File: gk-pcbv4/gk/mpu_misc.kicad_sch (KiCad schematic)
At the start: 28 parts, among them J5 Conn_ARM_Cortex_Debug_ETM_20, SW1 SW_Push, SW2 DS04-254-[12]-04BK-SMT, U5 STM32MP255DAI3, Y1 24MHz, Y2 CM8V-T1A-32.768kHz-12.5pF-20P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

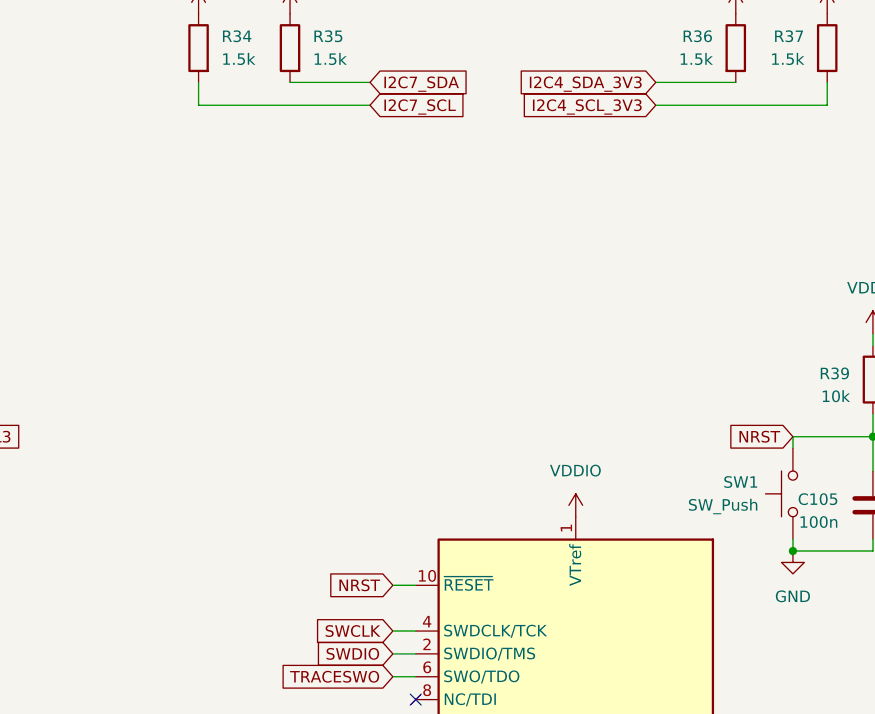
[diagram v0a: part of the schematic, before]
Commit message: add back-side 10 pin debug header
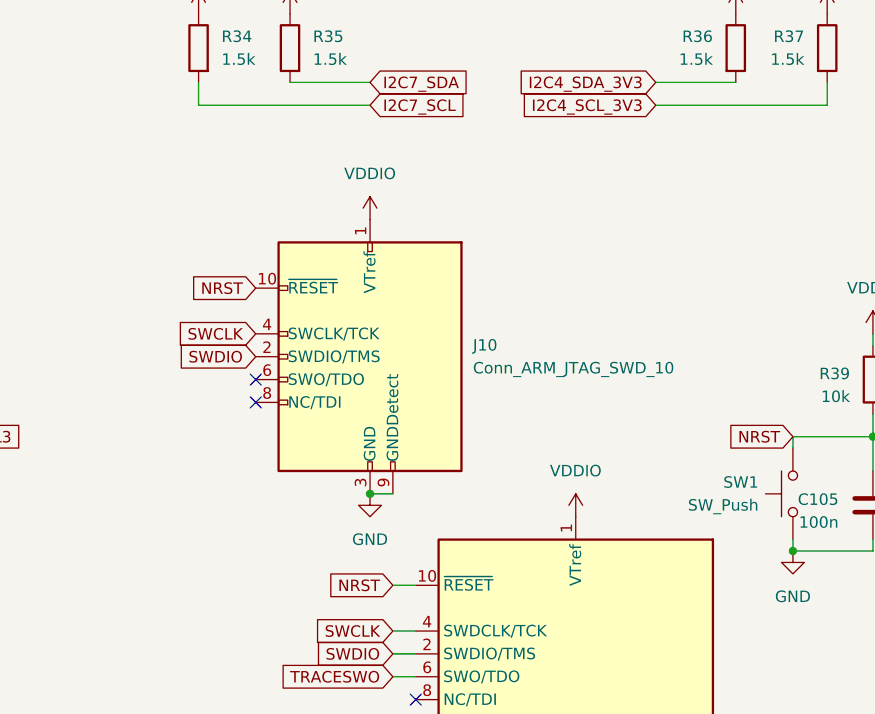
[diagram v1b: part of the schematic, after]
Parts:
- added J10: Conn_ARM_JTAG_SWD_10, Connector_PinHeader_1.27mm:PinHeader_2x05_P1.27mm_Vertical_SMD, symbol Connector:Conn_ARM_JTAG_SWD_10
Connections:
- net GND: now also J10.3 (GND), J10.5 (GND), J10.9 (GNDDetect)
- net NRST: now also J10.10 (~{RESET})
- net SWCLK: now also J10.4 (SWCLK/TCK)
- net SWDIO: now also J10.2 (SWDIO/TMS)
- net VDDIO: now also J10.1 (VTref)
- no-connect marks 32 -> 34

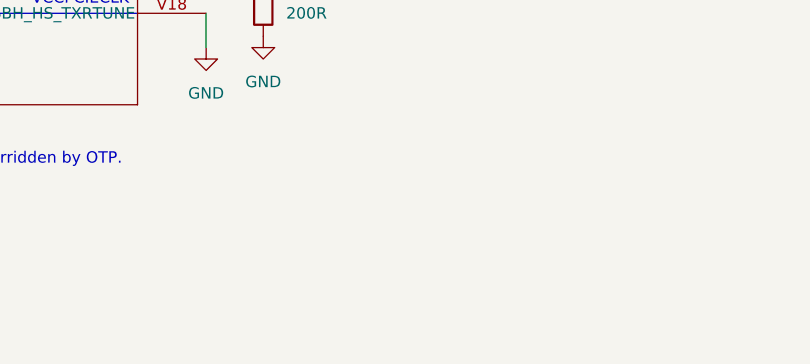
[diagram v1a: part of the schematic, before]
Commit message: Add UART6 out for debug
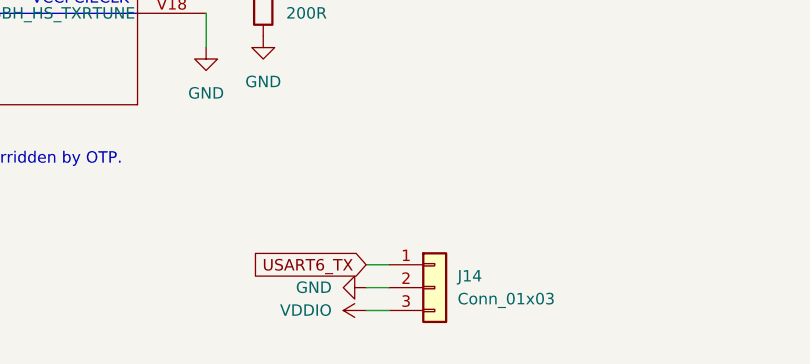
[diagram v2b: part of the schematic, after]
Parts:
- added J14: Conn_01x03, Connector_PinSocket_2.54mm:PinSocket_1x03_P2.54mm_Vertical, symbol Connector_Generic:Conn_01x03
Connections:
- net GND: now also J14.2 (Pin_2)
- net VDDIO: now also J14.3 (Pin_3)
- new net USART6_TX: J14.1 (Pin_1)

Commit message: pcb order 20251115
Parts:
- removed R42, R43, R44: 1k, Resistor_SMD:R_0603_1608Metric, symbol Device:R
- removed SW2: DS04-254-[12]-04BK-SMT, Button_Switch_SMD:SW_DIP_SPSTx04_Slide_9.78x12.34mm_W8.61mm_P2.54mm, symbol Switch:SW_DIP_x04
- added SW2: SW_Push, Button_Switch_SMD:SW_SPST_PTS647_Sx38, symbol Switch:SW_Push
- SW1: footprint gk-pcbv3:Tactile Switch 6x3.5mm -> Button_Switch_SMD:SW_SPST_PTS647_Sx38
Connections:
- net BOOT3: now also SW2.2
- net VDDIO: now also R45.1; no longer R45.2
- new net: R45.2, SW2.1
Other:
- moved on the sheet: R45

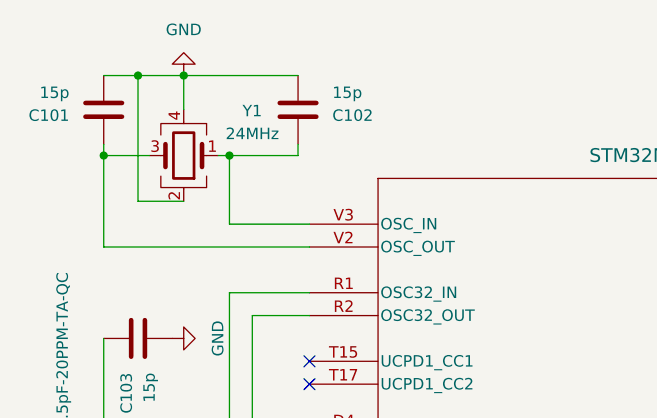
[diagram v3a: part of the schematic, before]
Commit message: Change HSE to 40 MHz as per EV1
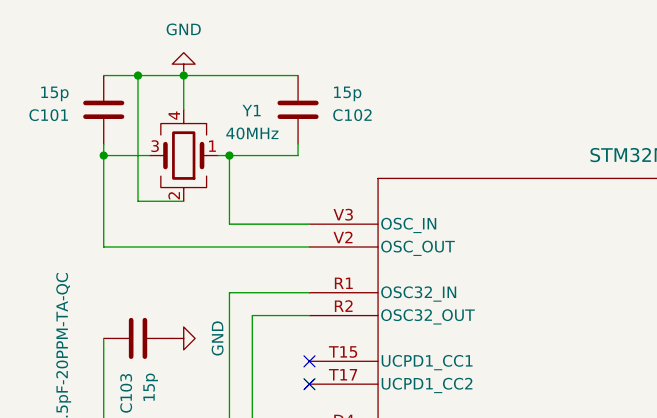
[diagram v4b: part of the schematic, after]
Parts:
- Y1: value 24MHz -> 40MHz
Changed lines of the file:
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@@
 			)
 		)
-		(property "Value" "24MHz"
+		(property "Value" "40MHz"
 			(at 39.37 26.7968 0)
 			(effects

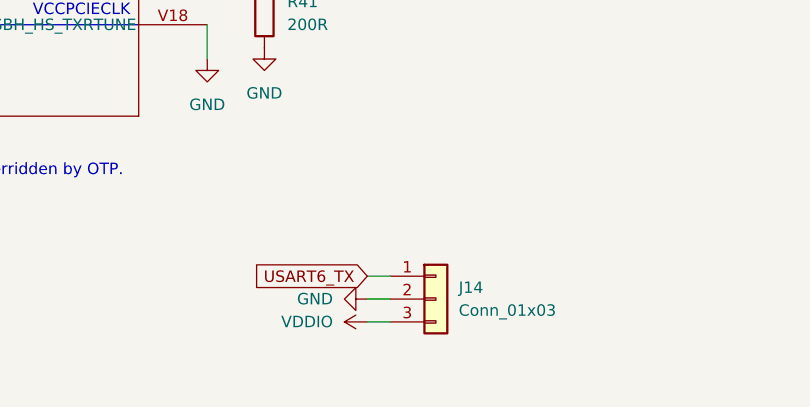
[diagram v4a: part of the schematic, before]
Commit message: add usart6 connection to schematic
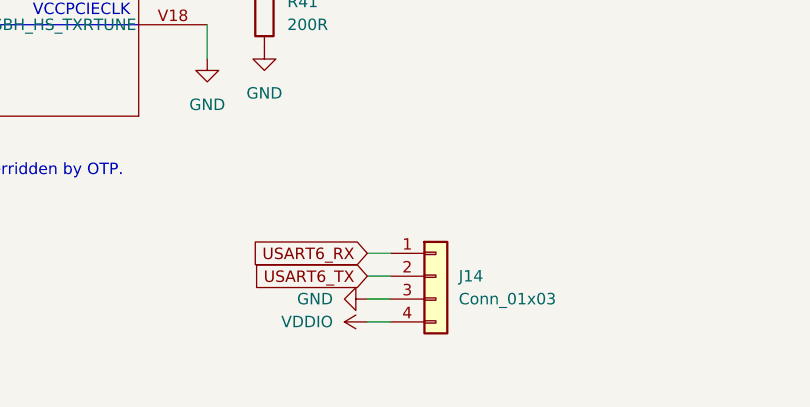
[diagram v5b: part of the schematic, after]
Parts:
- J14: symbol Connector_Generic:Conn_01x03 -> Connector_Generic:Conn_01x04
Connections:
- net GND: now also J14.3 (Pin_3); no longer J14.2 (Pin_2)
- net USART6_TX: now also J14.2 (Pin_2); no longer J14.1 (Pin_1)
- net VDDIO: now also J14.4 (Pin_4); no longer J14.3 (Pin_3)
- new net USART6_RX: J14.1 (Pin_1)
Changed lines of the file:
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@@
 	(wire
 		(pts
+			(xy 147.32 179.07) (xy 144.78 179.07)
+		)
+		(stroke
+			(width 0)
+			(type default)
+		)
+	)
+	(wire
+		(pts
 			(xy 236.22 157.48) (xy 242.57 157.48)
 		)
@@
 	(wire
 		(pts
-			(xy 144.78 173.99) (xy 147.32 173.99)
-		)
-		(stroke
-			(width 0)
-			(type default)
-		)
-	)
-	(wire
-		(pts
 			(xy 236.22 152.4) (xy 236.22 157.48)
 		)
@@
 	(wire
 		(pts
+			(xy 147.32 176.53) (xy 144.78 176.53)
+		)
+		(stroke
+			(width 0)
+			(type default)
+		)
+	)
+	(wire
+		(pts
 			(xy 233.68 152.4) (xy 233.68 158.75)
 		)
@@
 	(wire
 		(pts
-			(xy 147.32 176.53) (xy 144.78 176.53)
+			(xy 242.57 36.83) (xy 261.62 36.83)
 		)
 		(stroke
@@
 	(wire
 		(pts
-			(xy 242.57 36.83) (xy 261.62 36.83)
+			(xy 213.36 142.24) (xy 213.36 144.78)
 		)
 		(stroke
@@
 	(wire
 		(pts
-			(xy 213.36 142.24) (xy 213.36 144.78)
+			(xy 213.36 129.54) (xy 215.9 129.54)
 		)
 		(stroke
@@
 	(wire
 		(pts
-			(xy 213.36 129.54) (xy 215.9 129.54)
+			(xy 36.83 36.83) (xy 45.72 36.83)
 		)
 		(stroke
@@
 	(wire
 		(pts
-			(xy 36.83 36.83) (xy 45.72 36.83)
+			(xy 213.36 144.78) (xy 215.9 144.78)
 		)
 		(stroke
@@
 	(wire
 		(pts
-			(xy 213.36 144.78) (xy 215.9 144.78)
+			(xy 213.36 127) (xy 215.9 127)
 		)
 		(stroke
@@
 	(wire
 		(pts
-			(xy 213.36 127) (xy 215.9 127)
+			(xy 147.32 173.99) (xy 144.78 173.99)
 		)
 		(stroke
@@
 	(wire
 		(pts
-			(xy 213.36 132.08) (xy 215.9 132.08)
+			(xy 144.78 171.45) (xy 147.32 171.45)
 		)
 		(stroke
@@
 	(wire
 		(pts
-			(xy 144.78 179.07) (xy 147.32 179.07)
+			(xy 213.36 132.08) (xy 215.9 132.08)
 		)
 		(stroke
@@
 		)
 	)
+	(global_label "USART6_RX"
+		(shape input)
+		(at 144.78 171.45 180)
+		(fields_autoplaced yes)
+		(effects
+			(font
+				(size 1.27 1.27)
+			)
+			(justify right)
+		)
+		(property "Intersheetrefs" "${INTERSHEET_REFS}"
+			(at 131.272 171.45 0)
+			(effects
+				(font
+					(size 1.27 1.27)
+				)
+				(justify right)
+				(hide yes)
+			)
+		)
+	)
 	(global_label "TRACESWO"
 		(shape input)
@@
 	)
 	(symbol
-		(lib_id "Connector_Generic:Conn_01x03")
-		(at 152.4 176.53 0)
+		(lib_id "Connector_Generic:Conn_01x04")
+		(at 152.4 173.99 0)
 		(unit 1)
 		(exclude_from_sim no)
@@
 		(fields_autoplaced yes)
 		(property "Reference" "J14"
-			(at 154.94 175.2599 0)
+			(at 154.94 173.9899 0)
 			(effects
 				(font
@@
 		)
 		(property "Value" "Conn_01x03"
-			(at 154.94 177.7999 0)
+			(at 154.94 176.5299 0)
 			(effects
 				(font
@@
 		)
 		(property "Footprint" "Connector_PinSocket_2.54mm:PinSocket_1x03_P2.54mm_Vertical"
-			(at 152.4 176.53 0)
+			(at 152.4 173.99 0)
 			(effects
 				(font
@@
 		)
 		(property "Datasheet" "~"
-			(at 152.4 176.53 0)
+			(at 152.4 173.99 0)
 			(effects
 				(font
@@
 			)
 		)
-		(property "Description" "Generic connector, single row, 01x03, script generated (kicad-library-utils/schlib/autogen/connector/)"
-			(at 152.4 176.53 0)
+		(property "Description" "Generic connector, single row, 01x04, script generated (kicad-library-utils/schlib/autogen/connector/)"
+			(at 152.4 173.99 0)
 			(effects
 				(font
@@
 		(pin "3"
 		)
+		(pin "4"
+		)
 		(instances

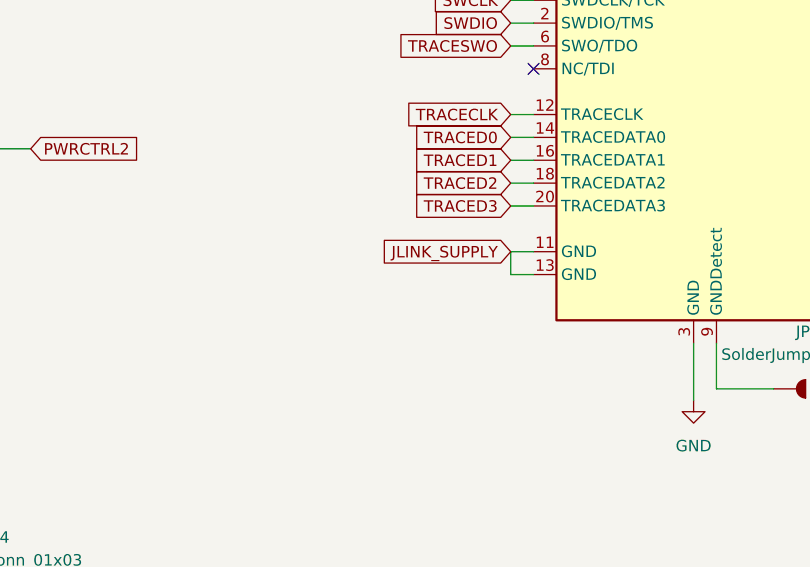
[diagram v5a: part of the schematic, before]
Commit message: Remove wakeupn mosfets in schematic
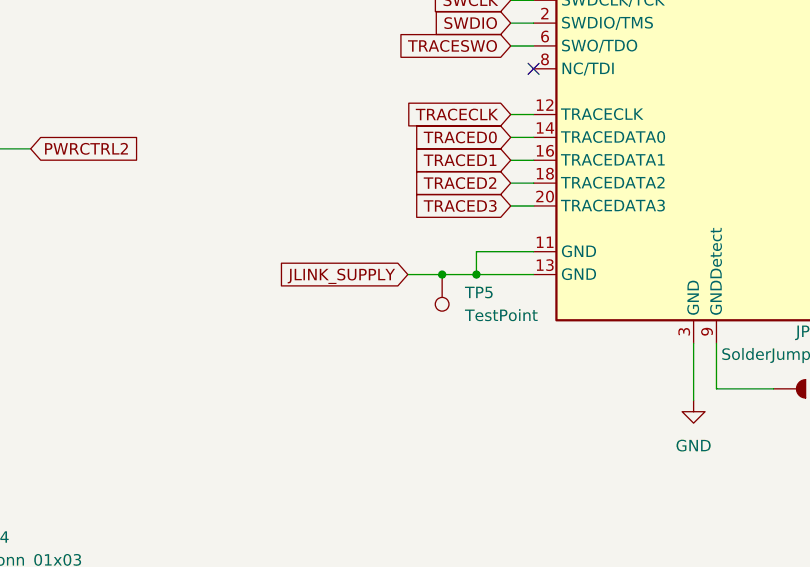
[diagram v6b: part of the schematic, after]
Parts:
- added TP5: TestPoint, Connector_PinHeader_2.54mm:PinHeader_1x01_P2.54mm_Vertical, symbol Connector:TestPoint
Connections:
- net JLINK_SUPPLY: now also TP5.1
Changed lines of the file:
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@@
 	)
 	(junction
+		(at 209.55 144.78)
+		(diameter 0)
+		(color 0 0 0 0)
+	)
+	(junction
 		(at 36.83 29.21)
 		(diameter 0)
@@
 	)
 	(junction
+		(at 205.74 144.78)
+		(diameter 0)
+		(color 0 0 0 0)
+	)
+	(junction
 		(at 152.4 130.81)
 		(diameter 0)
@@
 	(wire
 		(pts
+			(xy 209.55 142.24) (xy 215.9 142.24)
+		)
+		(stroke
+			(width 0)
+			(type default)
+		)
+	)
+	(wire
+		(pts
 			(xy 213.36 137.16) (xy 215.9 137.16)
 		)
@@
 	(wire
 		(pts
-			(xy 213.36 142.24) (xy 215.9 142.24)
+			(xy 201.93 144.78) (xy 205.74 144.78)
 		)
 		(stroke
@@
 	(wire
 		(pts
-			(xy 213.36 142.24) (xy 213.36 144.78)
+			(xy 209.55 144.78) (xy 209.55 142.24)
 		)
 		(stroke
@@
 	(wire
 		(pts
-			(xy 36.83 36.83) (xy 45.72 36.83)
+			(xy 209.55 144.78) (xy 215.9 144.78)
+		)
+		(stroke
+			(width 0)
+			(type default)
+		)
+	)
+	(wire
+		(pts
+			(xy 205.74 144.78) (xy 209.55 144.78)
 		)
 		(stroke
@@
 	(wire
 		(pts
-			(xy 213.36 144.78) (xy 215.9 144.78)
+			(xy 36.83 36.83) (xy 45.72 36.83)
 		)
 		(stroke
@@
 	(global_label "JLINK_SUPPLY"
 		(shape input)
-		(at 213.36 142.24 180)
+		(at 201.93 144.78 180)
 		(fields_autoplaced yes)
 		(effects
@@
 		)
 		(property "Intersheetrefs" "${INTERSHEET_REFS}"
-			(at 197.0095 142.24 0)
+			(at 185.5795 144.78 0)
 			(effects
 				(font
@@
 					(unit 1)
 				)
+			)
+		)
+	)
+	(symbol
+		(lib_id "Connector:TestPoint")
+		(at 205.74 144.78 180)
+		(unit 1)
+		(exclude_from_sim no)
+		(in_bom yes)
+		(on_board yes)
+		(dnp no)
+		(fields_autoplaced yes)
+		(property "Reference" "TP5"
+			(at 208.28 146.8119 0)
+			(effects
+				(font
+					(size 1.27 1.27)
+				)
+				(justify right)
+			)
+		)
+		(property "Value" "TestPoint"
+			(at 208.28 149.3519 0)
+			(effects
+				(font
+					(size 1.27 1.27)
+				)
+				(justify right)
+			)
+		)
+		(property "Footprint" "Connector_PinHeader_2.54mm:PinHeader_1x01_P2.54mm_Vertical"
+			(at 200.66 144.78 0)
+			(effects
+				(font
+					(size 1.27 1.27)
+				)
+				(hide yes)
+			)
+		)
+		(property "Datasheet" "~"
+			(at 200.66 144.78 0)
+			(effects
+				(font
+					(size 1.27 1.27)
+				)
+				(hide yes)
+			)
+		)
+		(property "Description" "test point"
+			(at 205.74 144.78 0)
+			(effects
+				(font
+					(size 1.27 1.27)
+				)
+				(hide yes)
+			)
+		)
+		(pin "1"
+		)
+		(instances
+			(project "gk"
+				(path "/a049c72e-5361-408c-ab21-661d491fee9d/2403dd54-21d5-4af4-8b44-b803e4ca621d"
+					(reference "TP5")
+					(unit 1)
+				)

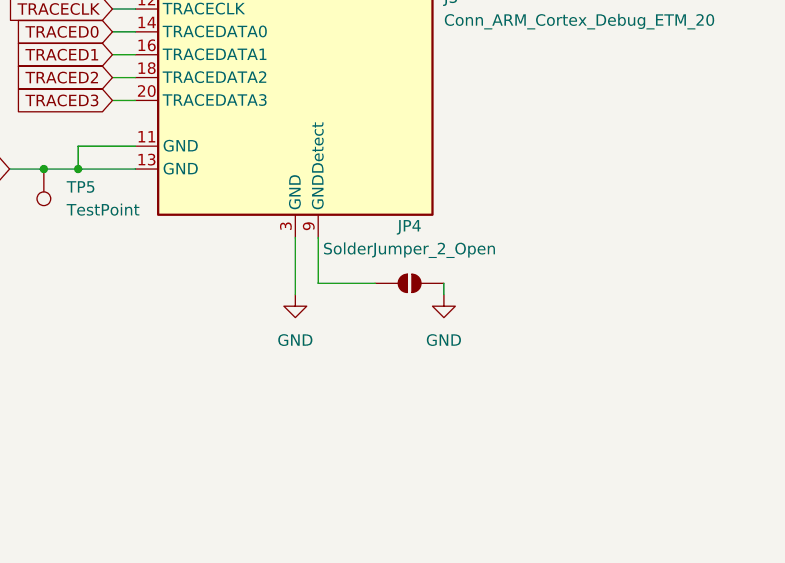
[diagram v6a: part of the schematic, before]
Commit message: remove solder bridges
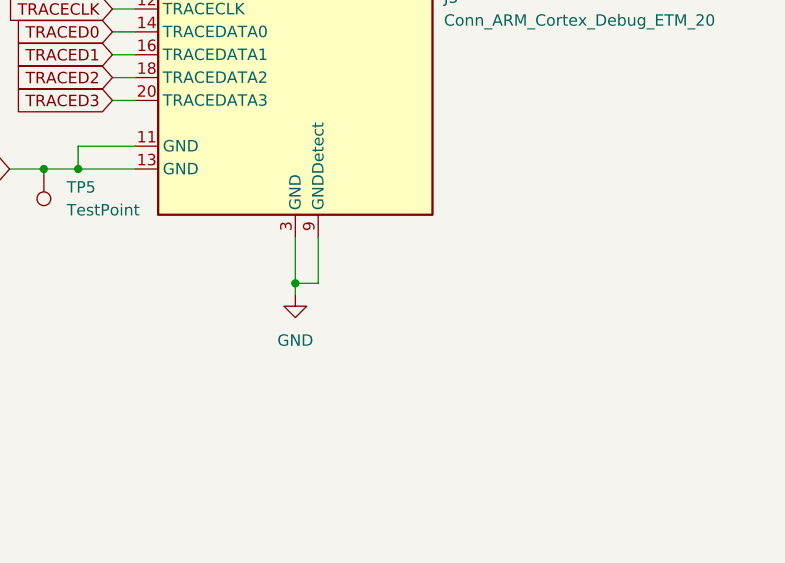
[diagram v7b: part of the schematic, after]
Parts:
- removed JP4: SolderJumper_2_Open, Jumper:SolderJumper-2_P1.3mm_Open_TrianglePad1.0x1.5mm, symbol Jumper:SolderJumper_2_Open
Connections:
- net GND: now also J5.9 (GNDDetect)
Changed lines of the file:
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@@
 	)
 	(junction
+		(at 233.68 157.48)
+		(diameter 0)
+		(color 0 0 0 0)
+	)
+	(junction
 		(at 26.67 20.32)
 		(diameter 0)
@@
 	(wire
 		(pts
+			(xy 233.68 157.48) (xy 236.22 157.48)
+		)
+		(stroke
+			(width 0)
+			(type default)
+		)
+	)
+	(wire
+		(pts
 			(xy 261.62 36.83) (xy 261.62 34.29)
 		)
@@
 	(wire
 		(pts
-			(xy 236.22 157.48) (xy 242.57 157.48)
-		)
-		(stroke
-			(width 0)
-			(type default)
-		)
-	)
-	(wire
-		(pts
 			(xy 22.86 67.31) (xy 22.86 78.74)
 		)
@@
 	(wire
 		(pts
+			(xy 233.68 157.48) (xy 233.68 158.75)
+		)
+		(stroke
+			(width 0)
+			(type default)
+		)
+	)
+	(wire
+		(pts
 			(xy 261.62 55.88) (xy 261.62 53.34)
 		)
@@
 	(wire
 		(pts
-			(xy 233.68 152.4) (xy 233.68 158.75)
+			(xy 233.68 152.4) (xy 233.68 157.48)
 		)
 		(stroke
@@
 	(wire
 		(pts
-			(xy 250.19 157.48) (xy 250.19 158.75)
-		)
-		(stroke
-			(width 0)
-			(type default)
-		)
-	)
-	(wire
-		(pts
 			(xy 266.7 96.52) (xy 266.7 92.71)
 		)
@@
 	)
 	(symbol
-		(lib_id "Jumper:SolderJumper_2_Open")
-		(at 246.38 157.48 0)
-		(unit 1)
-		(exclude_from_sim no)
-		(in_bom no)
-		(on_board yes)
-		(dnp no)
-		(fields_autoplaced yes)
-		(property "Reference" "JP4"
-			(at 246.38 151.13 0)
-			(effects
-				(font
-					(size 1.27 1.27)
-				)
-			)
-		)
-		(property "Value" "SolderJumper_2_Open"
-			(at 246.38 153.67 0)
-			(effects
-				(font
-					(size 1.27 1.27)
-				)
-			)
-		)
-		(property "Footprint" "Jumper:SolderJumper-2_P1.3mm_Open_TrianglePad1.0x1.5mm"
-			(at 246.38 157.48 0)
-			(effects
-				(font
-					(size 1.27 1.27)
-				)
-				(hide yes)
-			)
-		)
-		(property "Datasheet" "~"
-			(at 246.38 157.48 0)
-			(effects
-				(font
-					(size 1.27 1.27)
-				)
-				(hide yes)
-			)
-		)
-		(property "Description" "Solder Jumper, 2-pole, open"
-			(at 246.38 157.48 0)
-			(effects
-				(font
-					(size 1.27 1.27)
-				)
-				(hide yes)
-			)
-		)
-		(pin "1"
-		)
-		(pin "2"
-		)
-		(instances
-			(project ""
-				(path "/a049c72e-5361-408c-ab21-661d491fee9d/2403dd54-21d5-4af4-8b44-b803e4ca621d"
-					(reference "JP4")
-					(unit 1)
-				)
-			)
-		)
-	)
-	(symbol
 		(lib_id "power:VDD")
 		(at 144.78 179.07 90)
@@
 					(unit 1)
 				)
-			)
-		)
-	)
-	(symbol
-		(lib_id "power:GND")
-		(at 250.19 158.75 0)
-		(unit 1)
-		(exclude_from_sim no)
-		(in_bom yes)
-		(on_board yes)
-		(dnp no)
-		(fields_autoplaced yes)
-		(property "Reference" "#PWR0301"
-			(at 250.19 165.1 0)
-			(effects
-				(font
-					(size 1.27 1.27)
-				)
-				(hide yes)
-			)
-		)
-		(property "Value" "GND"
-			(at 250.19 163.83 0)
-			(effects
-				(font
-					(size 1.27 1.27)
-				)
-			)
-		)
-		(property "Footprint" ""
-			(at 250.19 158.75 0)
-			(effects
-				(font
-					(size 1.27 1.27)
-				)
-				(hide yes)
-			)
-		)
-		(property "Datasheet" ""
-			(at 250.19 158.75 0)
-			(effects
-				(font
-					(size 1.27 1.27)
-				)
-				(hide yes)
-			)
-		)
-		(property "Description" "Power symbol creates a global label with name \"GND\" , ground"
-			(at 250.19 158.75 0)
-			(effects
-				(font
-					(size 1.27 1.27)
-				)
-				(hide yes)
-			)
-		)
-		(pin "1"
-		)
-		(instances
-			(project "gk"
-				(path "/a049c72e-5361-408c-ab21-661d491fee9d/2403dd54-21d5-4af4-8b44-b803e4ca621d"
-					(reference "#PWR0301")
-					(unit 1)
-				)

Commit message: update pcb routing based on new v2 changes
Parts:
- J14: footprint Connector_PinSocket_2.54mm:PinSocket_1x03_P2.54mm_Vertical -> Connector_PinHeader_2.54mm:PinHeader_1x04_P2.54mm_Vertical
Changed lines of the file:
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@@
 			)
 		)
-		(property "Footprint" "Connector_PinSocket_2.54mm:PinSocket_1x03_P2.54mm_Vertical"
+		(property "Footprint" "Connector_PinHeader_2.54mm:PinHeader_1x04_P2.54mm_Vertical"
 			(at 152.4 173.99 0)
 			(effects
